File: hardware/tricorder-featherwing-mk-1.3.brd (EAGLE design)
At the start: 50.8 x 22.9 mm, 7 parts

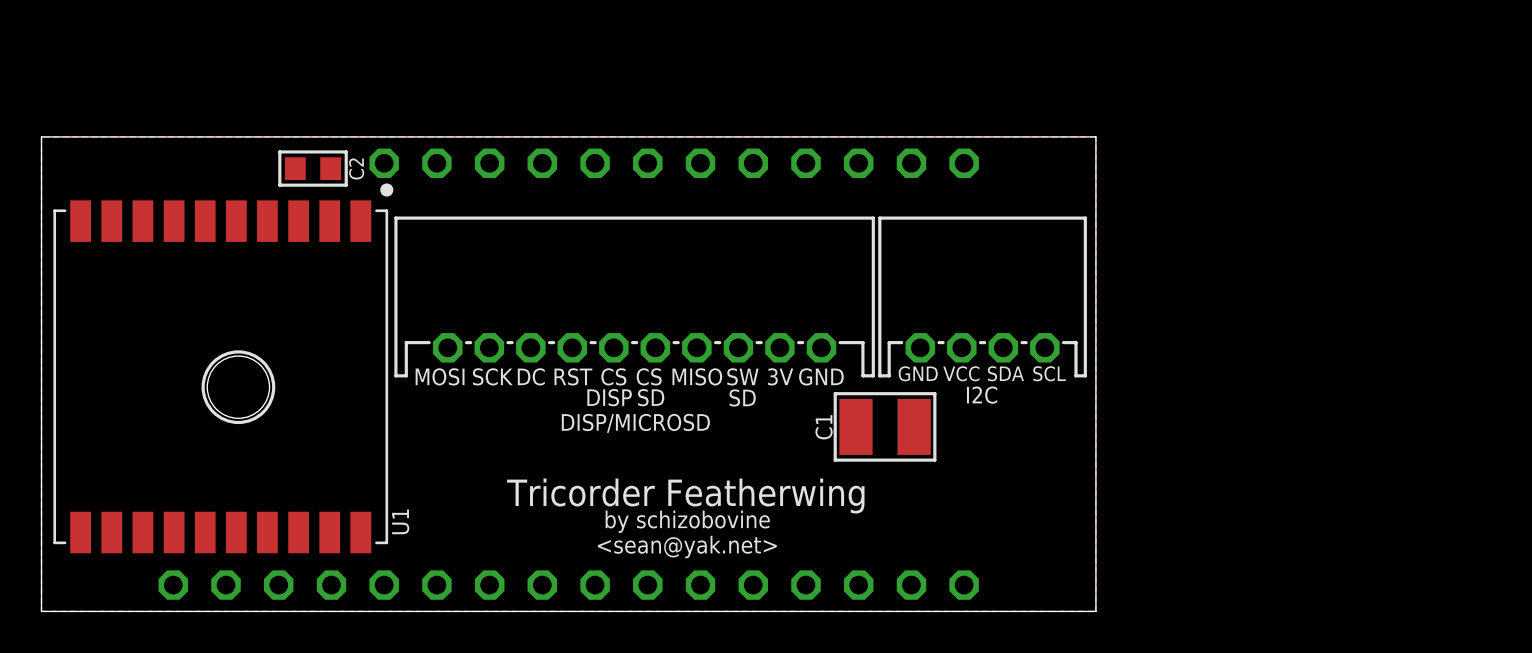
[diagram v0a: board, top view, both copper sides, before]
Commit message: more layout playing around for the jst version
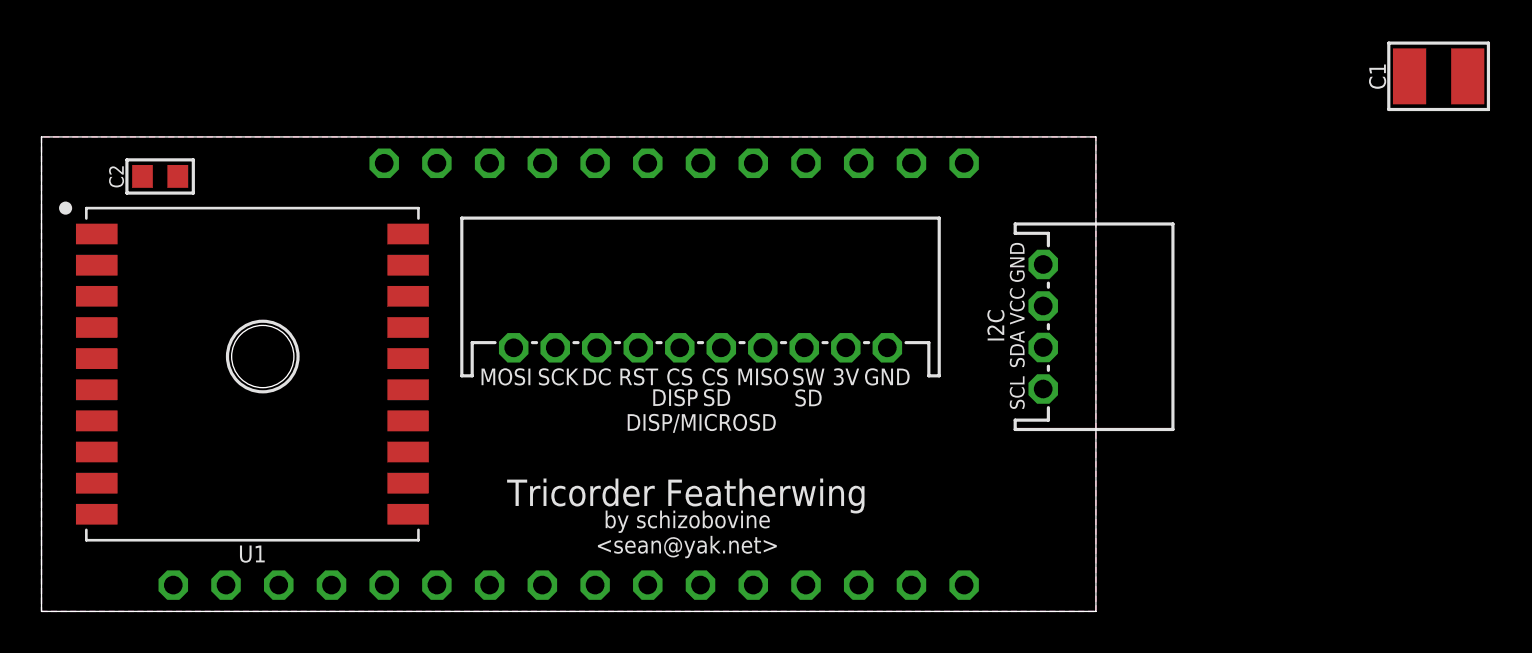
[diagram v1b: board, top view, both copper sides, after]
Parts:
- moved C1 31.6 mm to (67.3, 25.8)
- moved C2 7.38 mm to (5.71, 21.0), turned to 0 degrees
- moved DISP/MICROSD 3.18 mm to (31.8, 12.7)
- moved I2C 3.09 mm to (48.3, 13.7), turned to 270 degrees
- moved U1 1.53 mm to (10.2, 11.4), turned to 0 degrees

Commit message: jst version off to fab
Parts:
- removed U1: (no value), a_parts:FGPMMOPA6H
- added C3: 10uF, a_parts:C1210
- added GPS: (no value), a_parts:FGPMMOPA6H
- I2C: value M04-I2CJST-4-PH-RA-CENTERED -> M04-I2CPTH-0.1IN-CENTERED; device a_parts:1X04-JST-PH-RA-PTH-I2C-CENTERED -> a_parts:1X04-PTH-VERT-I2C-CENTERED
- moved I2C 38.9 mm to (10.2, 21.3), turned to 0 degrees
- moved C1 29.6 mm to (42.5, 9.53)
- moved C2 5.99 mm to (2.54, 15.9), turned to 270 degrees
- moved DISP/MICROSD 2.84 mm to (34.3, 14.0)
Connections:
- net 3.3V: now also C3.1, DISP/MICROSD.9, GPS.P$1, I2C.VCC; no longer I2C.2, U1.P$1
- net DISP_CS: now also DISP/MICROSD.5, FEATHERWING.A3; no longer FEATHERWING.11
- net DISP_DC: now also DISP/MICROSD.3, FEATHERWING.A1; no longer FEATHERWING.10
- net DISP_RST: now also DISP/MICROSD.4, FEATHERWING.A2; no longer FEATHERWING.A5
- net GND: now also C3.2, DISP/MICROSD.10, GPS.P$12, GPS.P$19, GPS.P$3, GPS.P$8, I2C.GND; no longer I2C.1, U1.P$12, U1.P$19, U1.P$3, U1.P$8
- net GPS_RX: now also FEATHERWING.12, GPS.P$10; no longer U1.P$10
- net GPS_TX: now also FEATHERWING.13, GPS.P$9; no longer U1.P$9
- net MISO: now also DISP/MICROSD.7
- net MOSI: now also DISP/MICROSD.1
- net SCK: now also DISP/MICROSD.2
- net SCL: now also I2C.SCL; no longer I2C.4
- net SDA: now also I2C.SDA; no longer I2C.3
- net SD_CS: now also DISP/MICROSD.6
- net SD_SW: now also DISP/MICROSD.8, FEATHERWING.A5; no longer FEATHERWING.A3
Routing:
- net 3.3V: track 0.00 -> 72.0 mm
- net SDA: track 0.00 -> 36.2 mm
- net GPS_RX: track 0.00 -> 32.5 mm
- net SCL: track 0.00 -> 30.0 mm
- net GPS_TX: track 0.00 -> 29.3 mm
- net SCK: track 0.00 -> 23.0 mm
- net DISP_DC: track 0.00 -> 16.9 mm
- net SD_SW: track 0.00 -> 16.9 mm
- net DISP_RST: track 0.00 -> 16.7 mm
- net DISP_CS: track 0.00 -> 16.5 mm
- net MOSI: track 0.00 -> 16.4 mm
- net SD_CS: track 0.00 -> 16.3 mm
- net MISO: track 0.00 -> 12.9 mm
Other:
- outline, holes or cut-outs redrawn
